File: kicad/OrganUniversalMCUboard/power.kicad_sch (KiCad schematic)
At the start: 8 parts, among them J1 VIN input (12-15V), J10 5V out, J2 EXT 5V In/out

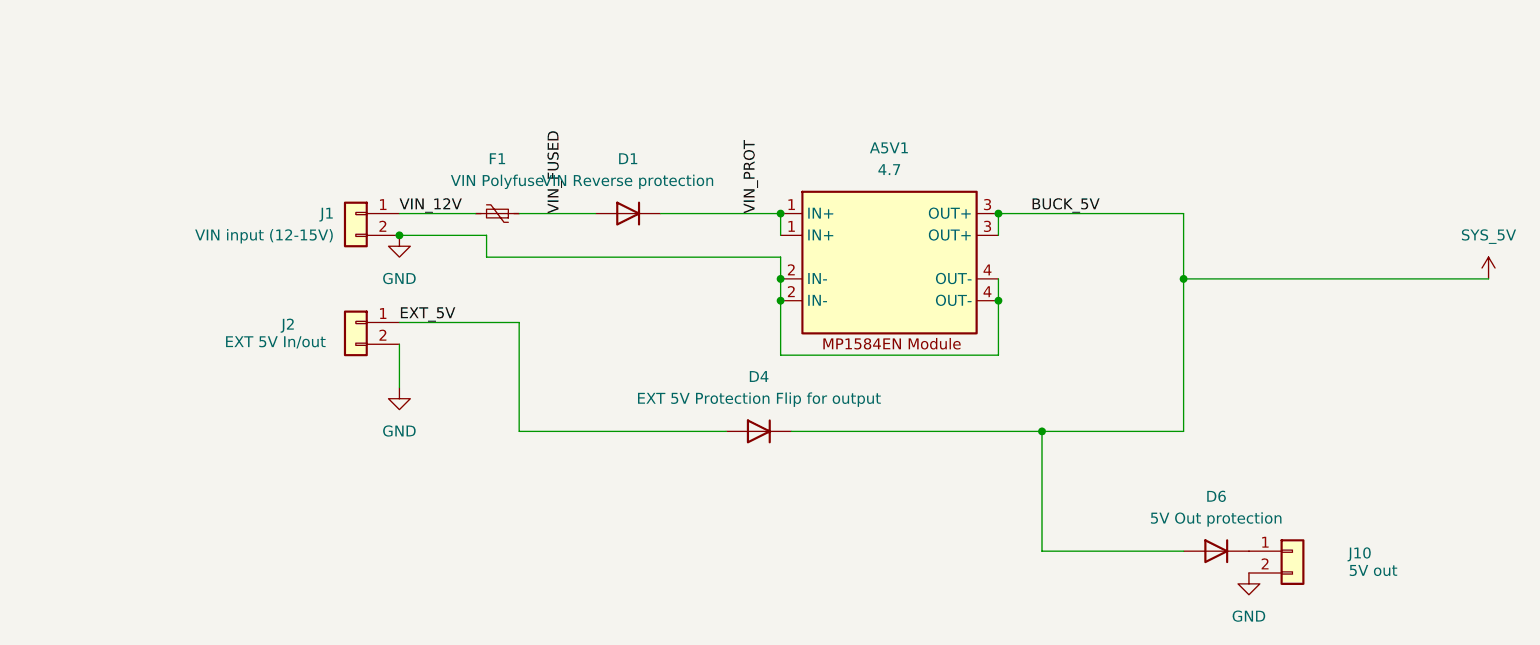
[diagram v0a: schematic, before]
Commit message: Finishing MCU board and lots of chimes updates
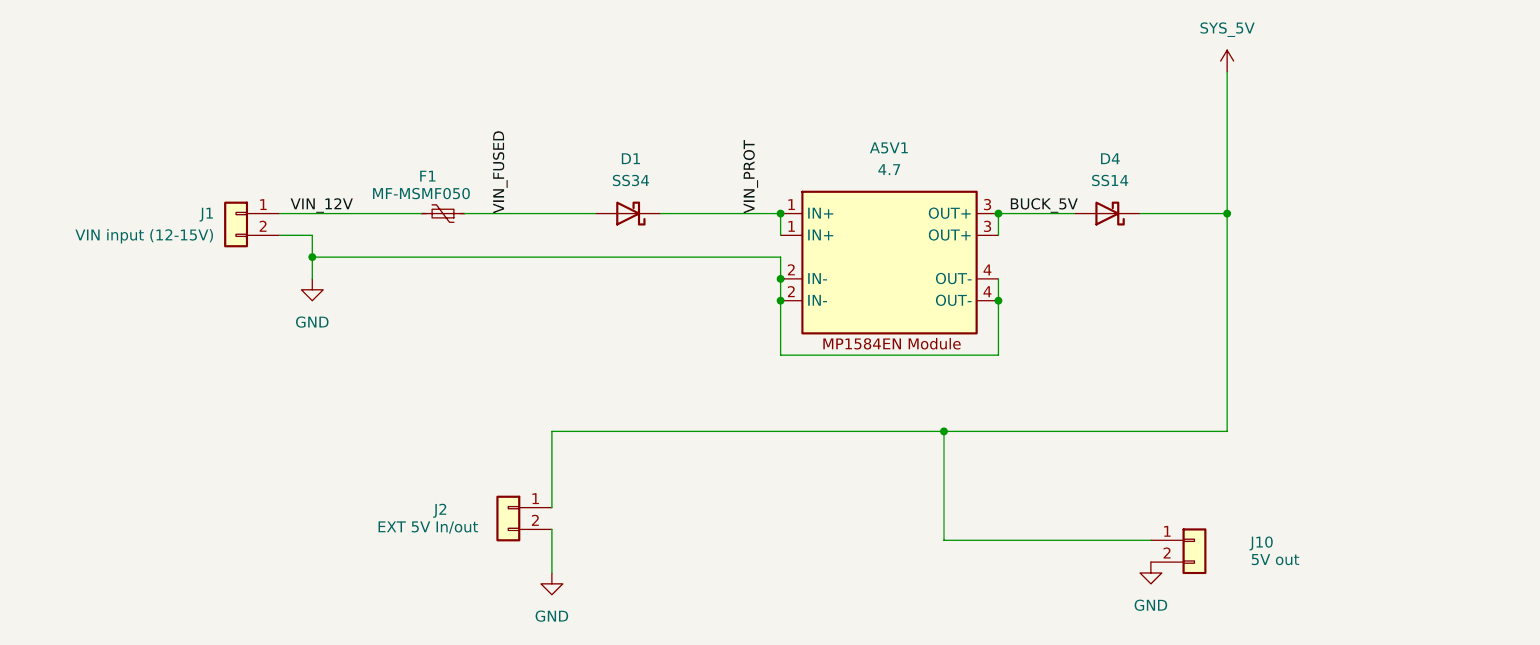
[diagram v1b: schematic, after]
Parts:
- removed D1: VIN Reverse protection, symbol Device:D
- removed D4: EXT 5V Protection Flip for output, symbol Device:D
- removed D6: 5V Out protection, symbol Device:D
- added D1: SS34, Diode_SMD:D_SMA, symbol Diode:SS34
- added D4: SS14, Diode_SMD:D_SMA, symbol Diode:SS14
- F1: value VIN Polyfuse -> MF-MSMF050; footprint (none) -> Fuse:Fuse_1812_4532Metric
- J1, J10, J2: footprint (none) -> Connector_JST:JST_PH_B2B-PH-K_1x02_P2.00mm_Vertical
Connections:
- net EXT_5V is gone; now on net SYS_5V: J2.1 (Pin_1)
- net SYS_5V: now also J10.1 (Pin_1), D4.1 (K); no longer A5V1.3 (OUT+)
- net VIN_FUSED: now also D1.2 (A)
- net VIN_PROT: now also D1.1 (K)
- new net BUCK_5V: A5V1.3 (OUT+), D4.2 (A)
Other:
- moved on the sheet: F1, J1, J10, J2
